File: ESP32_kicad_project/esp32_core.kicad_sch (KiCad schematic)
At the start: 15 parts, among them U2 ESP32-WROOM-32E

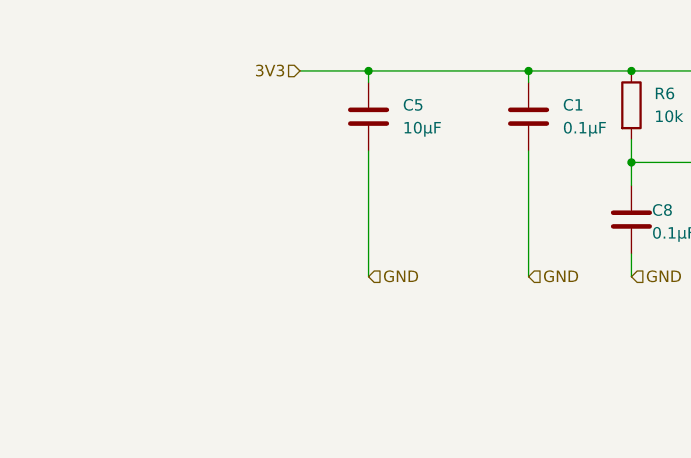
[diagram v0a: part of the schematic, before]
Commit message: added extra decoupling caps on the esp32 core 3V3 input
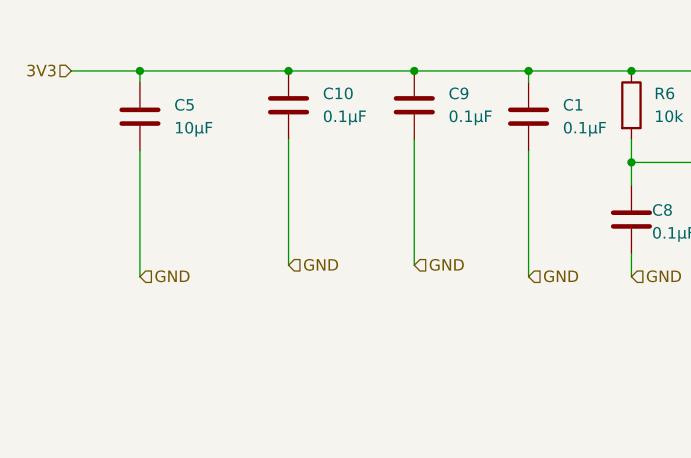
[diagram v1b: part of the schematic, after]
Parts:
- added C10, C9: 0.1µF, Capacitor_SMD:C_0603_1608Metric, symbol Device:C
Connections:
- net 3V3: now also C10.1, C9.1
- net GND: now also C10.2, C9.2
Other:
- moved on the sheet: C5
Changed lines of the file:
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@@
+	)
+	(junction
+		(at 64.77 55.88)
+		(diameter 0)
+		(color 0 0 0 0)
 	)
 	(junction
@@
 	)
 	(junction
-		(at 59.69 55.88)
+		(at 34.29 55.88)
 		(diameter 0)
 		(color 0 0 0 0)
@@
 	)
 	(junction
+		(at 50.8 55.88)
+		(diameter 0)
+		(color 0 0 0 0)
+	)
+	(junction
 		(at 88.9 66.04)
 		(diameter 0)
@@
 	(wire
 		(pts
-			(xy 59.69 55.88) (xy 59.69 57.15)
+			(xy 34.29 55.88) (xy 34.29 57.15)
 		)
 		(stroke
@@
 	(wire
 		(pts
+			(xy 64.77 55.88) (xy 77.47 55.88)
+		)
+		(stroke
+			(width 0)
+			(type default)
+		)
+	)
+	(wire
+		(pts
 			(xy 143.51 66.04) (xy 147.32 66.04)
 		)
@@
 	(wire
 		(pts
-			(xy 52.07 55.88) (xy 59.69 55.88)
+			(xy 26.67 55.88) (xy 34.29 55.88)
+		)
+		(stroke
+			(width 0)
+			(type default)
+		)
+	)
+	(wire
+		(pts
+			(xy 64.77 63.5) (xy 64.77 77.47)
 		)
 		(stroke
@@
 	(wire
 		(pts
+			(xy 50.8 63.5) (xy 50.8 77.47)
+		)
+		(stroke
+			(width 0)
+			(type default)
+		)
+	)
+	(wire
+		(pts
 			(xy 88.9 66.04) (xy 88.9 63.5)
 		)
@@
 	(wire
 		(pts
-			(xy 59.69 55.88) (xy 77.47 55.88)
+			(xy 34.29 55.88) (xy 50.8 55.88)
 		)
 		(stroke
@@
 	(wire
 		(pts
-			(xy 59.69 64.77) (xy 59.69 78.74)
+			(xy 34.29 64.77) (xy 34.29 78.74)
 		)
 		(stroke
@@
 		(pts
 			(xy 110.49 66.04) (xy 111.76 66.04)
+		)
+		(stroke
+			(width 0)
+			(type default)
+		)
+	)
+	(wire
+		(pts
+			(xy 50.8 55.88) (xy 64.77 55.88)
 		)
 		(stroke
@@
 	(hierarchical_label "GND"
 		(shape input)
-		(at 59.69 78.74 0)
+		(at 34.29 78.74 0)
 		(effects
 			(font
@@
 		)
 	)
+	(hierarchical_label "GND"
+		(shape input)
+		(at 50.8 77.47 0)
+		(effects
+			(font
+				(size 1.27 1.27)
+			)
+			(justify left)
+		)
+	)
 	(hierarchical_label "IO17"
 		(shape bidirectional)
@@
 	(hierarchical_label "3V3"
 		(shape input)
-		(at 52.07 55.88 180)
+		(at 26.67 55.88 180)
 		(effects
 			(font
@@
 		(shape input)
 		(at 143.51 64.77 0)
+		(effects
+			(font
+				(size 1.27 1.27)
+			)
+			(justify left)
+		)
+	)
+	(hierarchical_label "GND"
+		(shape input)
+		(at 64.77 77.47 0)
 		(effects
 			(font
@@
 	)
 	(symbol
+		(lib_id "Device:C")
+		(at 64.77 59.69 0)
+		(unit 1)
+		(exclude_from_sim no)
+		(in_bom yes)
+		(on_board yes)
+		(dnp no)
+		(fields_autoplaced yes)
+		(property "Reference" "C9"
+			(at 68.58 58.4199 0)
+			(effects
+				(font
+					(size 1.27 1.27)
+				)
+				(justify left)
+			)
+		)
+		(property "Value" "0.1µF"
+			(at 68.58 60.9599 0)
+			(effects
+				(font
+					(size 1.27 1.27)
+				)
+				(justify left)
+			)
+		)
+		(property "Footprint" "Capacitor_SMD:C_0603_1608Metric"
+			(at 65.7352 63.5 0)
+			(effects
+				(font
+					(size 1.27 1.27)
+				)
+				(hide yes)
+			)
+		)
+		(property "Datasheet" "~"
+			(at 64.77 59.69 0)
+			(effects
+				(font
+					(size 1.27 1.27)
+				)
+				(hide yes)
+			)
+		)
+		(property "Description" "Unpolarized capacitor"
+			(at 64.77 59.69 0)
+			(effects
+				(font
+					(size 1.27 1.27)
+				)
+				(hide yes)
+			)
+		)
+		(pin "1"
+		)
+		(pin "2"
+		)
+		(instances
+			(project "ESP32_kicad_project"
+				(path "/8f7d6ecf-e535-4443-9266-fe4b2e9314d5/71ad0a68-ebcc-403d-8fb5-019c32511765"
+					(reference "C9")
+					(unit 1)
+				)
+			)
+		)
+	)
+	(symbol
 		(lib_id "Connector:TestPoint")
 		(at 96.52 66.04 0)
@@
 	)
 	(symbol
+		(lib_id "Device:C")
+		(at 50.8 59.69 0)
+		(unit 1)
+		(exclude_from_sim no)
+		(in_bom yes)
+		(on_board yes)
+		(dnp no)
+		(fields_autoplaced yes)
+		(property "Reference" "C10"
+			(at 54.61 58.4199 0)
+			(effects
+				(font
+					(size 1.27 1.27)
+				)
+				(justify left)
+			)
+		)
+		(property "Value" "0.1µF"
+			(at 54.61 60.9599 0)
+			(effects
+				(font
+					(size 1.27 1.27)
+				)
+				(justify left)
+			)
+		)
+		(property "Footprint" "Capacitor_SMD:C_0603_1608Metric"
+			(at 51.7652 63.5 0)
+			(effects
+				(font
+					(size 1.27 1.27)
+				)
+				(hide yes)
+			)
+		)
+		(property "Datasheet" "~"
+			(at 50.8 59.69 0)
+			(effects
+				(font
+					(size 1.27 1.27)
+				)
+				(hide yes)
+			)
+		)
+		(property "Description" "Unpolarized capacitor"
+			(at 50.8 59.69 0)
+			(effects
+				(font
+					(size 1.27 1.27)
+				)
+				(hide yes)
+			)
+		)
+		(pin "1"
+		)
+		(pin "2"
+		)
+		(instances
+			(project "ESP32_kicad_project"
+				(path "/8f7d6ecf-e535-4443-9266-fe4b2e9314d5/71ad0a68-ebcc-403d-8fb5-019c32511765"
+					(reference "C10")
+					(unit 1)
+				)
+			)
+		)
+	)
+	(symbol
 		(lib_id "Connector:TestPoint")
 		(at 188.7936 73.66 0)
@@
 	(symbol
 		(lib_id "Device:C")
-		(at 59.69 60.96 0)
+		(at 34.29 60.96 0)
 		(unit 1)
 		(exclude_from_sim no)
@@
 		(fields_autoplaced yes)
 		(property "Reference" "C5"
-			(at 63.5 59.6899 0)
+			(at 38.1 59.6899 0)
 			(effects
 				(font
@@
 		)
 		(property "Value" "10µF"
-			(at 63.5 62.2299 0)
+			(at 38.1 62.2299 0)
 			(effects
 				(font
@@
 		)
 		(property "Footprint" "Capacitor_SMD:C_0805_2012Metric"
-			(at 60.6552 64.77 0)
+			(at 35.2552 64.77 0)
 			(effects
 				(font
@@
 		)
 		(property "Datasheet" "~"
-			(at 59.69 60.96 0)
+			(at 34.29 60.96 0)
 			(effects
 				(font
@@
 		)
 		(property "Description" "Unpolarized capacitor"
-			(at 59.69 60.96 0)
-			(effects
-				(font
+			(at 34.29 60.96 0)
+			(effects
+				(font

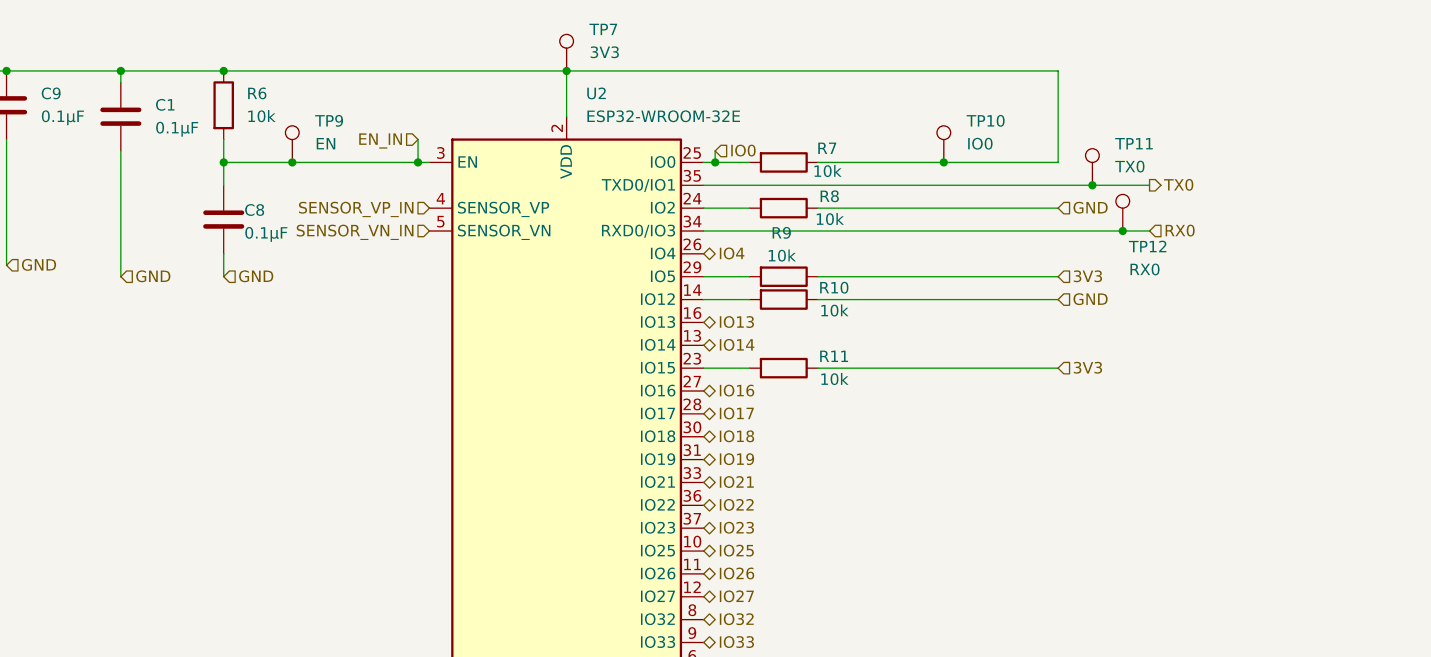
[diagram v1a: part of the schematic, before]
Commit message: added EN and IO0 switches, reset and boot, respectively
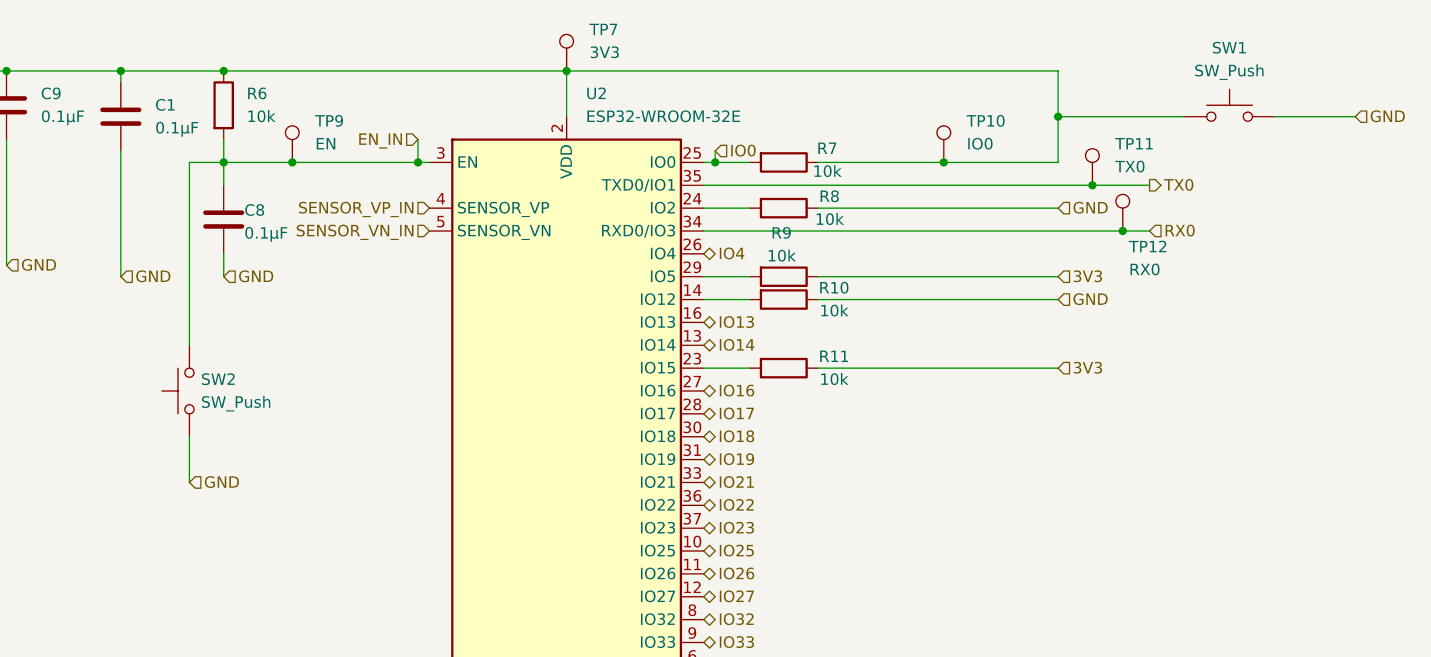
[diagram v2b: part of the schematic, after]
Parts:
- added SW1, SW2: SW_Push, symbol Switch:SW_Push
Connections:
- net 3V3: now also SW1.1
- net EN_IN: now also SW2.2
- net GND: now also SW1.2, SW2.1
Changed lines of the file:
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@@
+	)
+	(junction
+		(at 181.61 60.96)
+		(diameter 0)
+		(color 0 0 0 0)
 	)
 	(junction
@@
 	(wire
 		(pts
+			(xy 85.09 96.52) (xy 85.09 101.6)
+		)
+		(stroke
+			(width 0)
+			(type default)
+		)
+	)
+	(wire
+		(pts
 			(xy 188.7936 73.66) (xy 142.24 73.66)
 		)
@@
 	(wire
 		(pts
+			(xy 205.74 60.96) (xy 214.63 60.96)
+		)
+		(stroke
+			(width 0)
+			(type default)
+		)
+	)
+	(wire
+		(pts
 			(xy 154.94 78.74) (xy 181.61 78.74)
 		)
@@
 	(wire
 		(pts
+			(xy 181.61 60.96) (xy 181.61 55.88)
+		)
+		(stroke
+			(width 0)
+			(type default)
+		)
+	)
+	(wire
+		(pts
 			(xy 154.94 88.9) (xy 181.61 88.9)
 		)
@@
 	(wire
 		(pts
+			(xy 181.61 60.96) (xy 195.58 60.96)
+		)
+		(stroke
+			(width 0)
+			(type default)
+		)
+	)
+	(wire
+		(pts
 			(xy 191.77 68.58) (xy 185.42 68.58)
 		)
@@
 	(wire
 		(pts
+			(xy 85.09 66.04) (xy 88.9 66.04)
+		)
+		(stroke
+			(width 0)
+			(type default)
+		)
+	)
+	(wire
+		(pts
 			(xy 191.77 73.66) (xy 188.7936 73.66)
 		)
@@
 	(wire
 		(pts
+			(xy 85.09 86.36) (xy 85.09 66.04)
+		)
+		(stroke
+			(width 0)
+			(type default)
+		)
+	)
+	(wire
+		(pts
 			(xy 168.91 66.04) (xy 181.61 66.04)
 		)
@@
 	(wire
 		(pts
-			(xy 181.61 66.04) (xy 181.61 55.88)
+			(xy 181.61 66.04) (xy 181.61 60.96)
 		)
 		(stroke
@@
 		)
 	)
+	(hierarchical_label "GND"
+		(shape input)
+		(at 214.63 60.96 0)
+		(effects
+			(font
+				(size 1.27 1.27)
+			)
+			(justify left)
+		)
+	)
 	(hierarchical_label "IO33"
 		(shape bidirectional)
@@
 		(shape bidirectional)
 		(at 142.24 111.76 0)
+		(effects
+			(font
+				(size 1.27 1.27)
+			)
+			(justify left)
+		)
+	)
+	(hierarchical_label "GND"
+		(shape input)
+		(at 85.09 101.6 0)
 		(effects
 			(font
@@
 	)
 	(symbol
+		(lib_id "Switch:SW_Push")
+		(at 85.09 91.44 90)
+		(unit 1)
+		(exclude_from_sim no)
+		(in_bom yes)
+		(on_board yes)
+		(dnp no)
+		(fields_autoplaced yes)
+		(property "Reference" "SW2"
+			(at 86.36 90.1699 90)
+			(effects
+				(font
+					(size 1.27 1.27)
+				)
+				(justify right)
+			)
+		)
+		(property "Value" "SW_Push"
+			(at 86.36 92.7099 90)
+			(effects
+				(font
+					(size 1.27 1.27)
+				)
+				(justify right)
+			)
+		)
+		(property "Footprint" ""
+			(at 80.01 91.44 0)
+			(effects
+				(font
+					(size 1.27 1.27)
+				)
+				(hide yes)
+			)
+		)
+		(property "Datasheet" "~"
+			(at 80.01 91.44 0)
+			(effects
+				(font
+					(size 1.27 1.27)
+				)
+				(hide yes)
+			)
+		)
+		(property "Description" "Push button switch, generic, two pins"
+			(at 85.09 91.44 0)
+			(effects
+				(font
+					(size 1.27 1.27)
+				)
+				(hide yes)
+			)
+		)
+		(pin "2"
+		)
+		(pin "1"
+		)
+		(instances
+			(project "ESP32_kicad_project"
+				(path "/8f7d6ecf-e535-4443-9266-fe4b2e9314d5/71ad0a68-ebcc-403d-8fb5-019c32511765"
+					(reference "SW2")
+					(unit 1)
+				)
+			)
+		)
+	)
+	(symbol
 		(lib_id "Device:R")
 		(at 151.13 66.04 270)
@@
 					(unit 1)
 				)
+			)
+		)
+	)
+	(symbol
+		(lib_id "Switch:SW_Push")
+		(at 200.66 60.96 0)
+		(unit 1)
+		(exclude_from_sim no)
+		(in_bom yes)
+		(on_board yes)
+		(dnp no)
+		(fields_autoplaced yes)
+		(property "Reference" "SW1"
+			(at 200.66 53.34 0)
+			(effects
+				(font
+					(size 1.27 1.27)
+				)
+			)
+		)
+		(property "Value" "SW_Push"
+			(at 200.66 55.88 0)
+			(effects
+				(font
+					(size 1.27 1.27)
+				)
+			)
+		)
+		(property "Footprint" ""
+			(at 200.66 55.88 0)
+			(effects
+				(font
+					(size 1.27 1.27)
+				)
+				(hide yes)
+			)
+		)
+		(property "Datasheet" "~"
+			(at 200.66 55.88 0)
+			(effects
+				(font
+					(size 1.27 1.27)
+				)
+				(hide yes)
+			)
+		)
+		(property "Description" "Push button switch, generic, two pins"
+			(at 200.66 60.96 0)
+			(effects
+				(font
+					(size 1.27 1.27)
+				)
+				(hide yes)
+			)
+		)
+		(pin "2"
+		)
+		(pin "1"
+		)
+		(instances
+			(project ""
+				(path "/8f7d6ecf-e535-4443-9266-fe4b2e9314d5/71ad0a68-ebcc-403d-8fb5-019c32511765"
+					(reference "SW1")
+					(unit 1)
+				)

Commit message: completed core, moving on to the usb-uart core
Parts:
- added J1: Conn_01x04_Pin, symbol Connector:Conn_01x04_Pin
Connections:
- net 3V3: now also J1.1 (Pin_1)
- net GND: now also J1.4 (Pin_4)
- net RX0: now also J1.3 (Pin_3)
- net TX0: now also J1.2 (Pin_2)
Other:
- title: (none) -> ESP32 DevBoard - ESP32 Core
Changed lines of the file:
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@@
 	(generator_version "9.0")
 	(paper "A4")
+	(title_block
+		(title "ESP32 DevBoard - ESP32 Core")
+		(date "2026-02-08")
+		(rev "v1.0")
+	)
 	(junction
 		(at 110.49 66.04)
@@
 	)
 	(junction
+		(at 205.74 68.58)
+		(diameter 0)
+		(color 0 0 0 0)
+	)
+	(junction
+		(at 205.74 73.66)
+		(diameter 0)
+		(color 0 0 0 0)
+	)
+	(junction
 		(at 168.91 66.04)
 		(diameter 0)
@@
 	(wire
 		(pts
+			(xy 205.74 71.12) (xy 205.74 73.66)
+		)
+		(stroke
+			(width 0)
+			(type default)
+		)
+	)
+	(wire
+		(pts
 			(xy 85.09 96.52) (xy 85.09 101.6)
 		)
@@
 	(wire
 		(pts
+			(xy 226.06 71.12) (xy 215.9 71.12)
+		)
+		(stroke
+			(width 0)
+			(type default)
+		)
+	)
+	(wire
+		(pts
 			(xy 88.9 66.04) (xy 96.52 66.04)
 		)
@@
 	(wire
 		(pts
-			(xy 191.77 68.58) (xy 185.42 68.58)
+			(xy 215.9 73.66) (xy 205.74 73.66)
+		)
+		(stroke
+			(width 0)
+			(type default)
+		)
+	)
+	(wire
+		(pts
+			(xy 207.01 64.77) (xy 205.74 64.77)
 		)
 		(stroke
@@
 	(wire
 		(pts
+			(xy 226.06 53.34) (xy 226.06 66.04)
+		)
+		(stroke
+			(width 0)
+			(type default)
+		)
+	)
+	(wire
+		(pts
+			(xy 205.74 68.58) (xy 226.06 68.58)
+		)
+		(stroke
+			(width 0)
+			(type default)
+		)
+	)
+	(wire
+		(pts
+			(xy 205.74 68.58) (xy 185.42 68.58)
+		)
+		(stroke
+			(width 0)
+			(type default)
+		)
+	)
+	(wire
+		(pts
 			(xy 142.24 78.74) (xy 147.32 78.74)
 		)
@@
 	(wire
 		(pts
+			(xy 226.06 73.66) (xy 226.06 87.63)
+		)
+		(stroke
+			(width 0)
+			(type default)
+		)
+	)
+	(wire
+		(pts
+			(xy 205.74 64.77) (xy 205.74 68.58)
+		)
+		(stroke
+			(width 0)
+			(type default)
+		)
+	)
+	(wire
+		(pts
 			(xy 64.77 55.88) (xy 77.47 55.88)
 		)
@@
 	(wire
 		(pts
+			(xy 205.74 73.66) (xy 188.7936 73.66)
+		)
+		(stroke
+			(width 0)
+			(type default)
+		)
+	)
+	(wire
+		(pts
 			(xy 26.67 55.88) (xy 34.29 55.88)
 		)
@@
 	(wire
 		(pts
-			(xy 191.77 73.66) (xy 188.7936 73.66)
+			(xy 207.01 71.12) (xy 205.74 71.12)
 		)
 		(stroke
@@
 	(wire
 		(pts
+			(xy 227.33 53.34) (xy 226.06 53.34)
+		)
+		(stroke
+			(width 0)
+			(type default)
+		)
+	)
+	(wire
+		(pts
 			(xy 88.9 55.88) (xy 127 55.88)
 		)
@@
 	(wire
 		(pts
+			(xy 215.9 71.12) (xy 215.9 73.66)
+		)
+		(stroke
+			(width 0)
+			(type default)
+		)
+	)
+	(wire
+		(pts
 			(xy 96.52 66.04) (xy 110.49 66.04)
 		)
@@
 		(pts
 			(xy 85.09 86.36) (xy 85.09 66.04)
+		)
+		(stroke
+			(width 0)
+			(type default)
+		)
+	)
+	(wire
+		(pts
+			(xy 226.06 87.63) (xy 227.33 87.63)
 		)
 		(stroke
@@
 	(hierarchical_label "RX0"
 		(shape input)
-		(at 191.77 73.66 0)
+		(at 207.01 71.12 0)
 		(effects
 			(font
@@
 		)
 	)
+	(hierarchical_label "GND"
+		(shape input)
+		(at 227.33 87.63 0)
+		(effects
+			(font
+				(size 1.27 1.27)
+			)
+			(justify left)
+		)
+	)
 	(hierarchical_label "SENSOR_VN_IN"
 		(shape input)
@@
 	(hierarchical_label "TX0"
 		(shape output)
-		(at 191.77 68.58 0)
+		(at 207.01 64.77 0)
 		(effects
 			(font
@@
 		(shape input)
 		(at 181.61 78.74 0)
+		(effects
+			(font
+				(size 1.27 1.27)
+			)
+			(justify left)
+		)
+	)
+	(hierarchical_label "3V3"
+		(shape input)
+		(at 227.33 53.34 0)
 		(effects
 			(font
@@
 					(unit 1)
 				)
+			)
+		)
+	)
+	(symbol
+		(lib_id "Connector:Conn_01x04_Pin")
+		(at 231.14 68.58 0)
+		(mirror y)
+		(unit 1)
+		(exclude_from_sim no)
+		(in_bom yes)
+		(on_board yes)
+		(dnp no)
+		(property "Reference" "J1"
+			(at 241.046 67.564 0)
+			(effects
+				(font
+					(size 1.27 1.27)
+				)
+			)
+		)
+		(property "Value" "Conn_01x04_Pin"
+			(at 241.046 70.104 0)
+			(effects
+				(font
+					(size 1.27 1.27)
+				)
+			)
+		)
+		(property "Footprint" ""
+			(at 231.14 68.58 0)
+			(effects
+				(font
+					(size 1.27 1.27)
+				)
+				(hide yes)
+			)
+		)
+		(property "Datasheet" "~"
+			(at 231.14 68.58 0)
+			(effects
+				(font
+					(size 1.27 1.27)
+				)
+				(hide yes)
+			)
+		)
+		(property "Description" "Generic connector, single row, 01x04, script generated"
+			(at 231.14 68.58 0)
+			(effects
+				(font
+					(size 1.27 1.27)
+				)
+				(hide yes)
+			)
+		)
+		(pin "3"
+		)
+		(pin "1"
+		)
+		(pin "2"
+		)
+		(pin "4"
+		)
+		(instances
+			(project ""
+				(path "/8f7d6ecf-e535-4443-9266-fe4b2e9314d5/71ad0a68-ebcc-403d-8fb5-019c32511765"
+					(reference "J1")
+					(unit 1)
+				)
